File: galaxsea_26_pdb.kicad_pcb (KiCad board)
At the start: 2 copper layers, 235.7 x 148.4 mm, 92 parts, among them J1 XT-30, J10 XT-30, J11 Conn_01x36, J12 XT-30, J13 XT-30, J14 XT-30, J15 XT-30, J16 XT-30, J17 XT-30, J18 XT-30, J19 Conn_01x36, J2 XT-30, J20 XT-90, J21 Conn_01x36, J22 XT-30, J23 XT-30, J24 XT-30, J25 XT-30, J26 Conn_01x36, J27 XT-30, J28 XT-30, J29 XT-30, J3 Conn_01x36, J30 XT-30, J31 B2B-XH, J32 B2B-XH, J33 XT-30, J34 XT-60, J35 XT-60, J36 XT-60, J37 XT-60, J4 Conn_01x36, J5 Conn_01x36, J6 XT-30, J7 XT-90, J8 XT-30, J9 XT-30, U1 TPS54531DDA, U2 TPS54531DDA

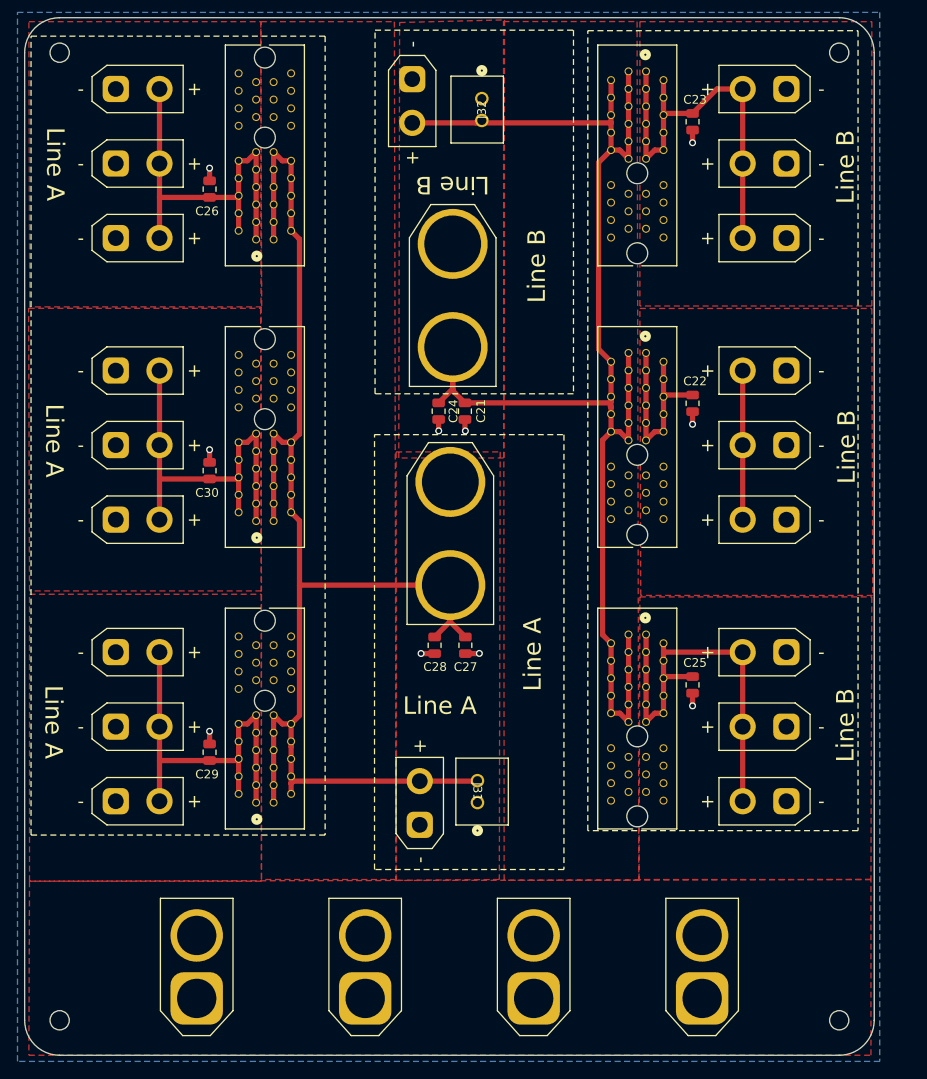
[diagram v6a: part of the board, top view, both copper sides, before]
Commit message: Switch ESC connectors to XT-30
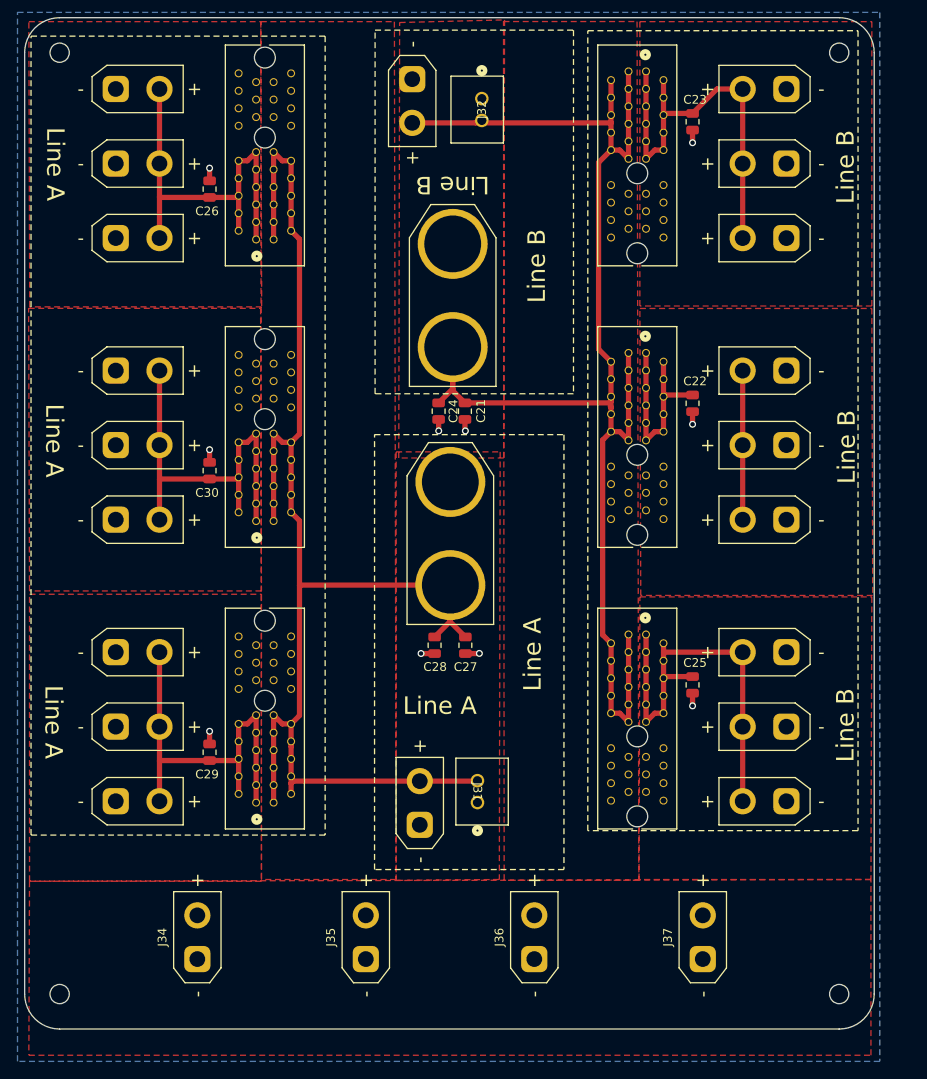
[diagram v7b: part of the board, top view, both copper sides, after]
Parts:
- J34, J35, J36, J37: value XT-60 -> XT-30; footprint footprints:AMASS_XT60-F_1x02_P7.20mm_Vertical -> Connector_AMASS:AMASS_XT30UPB-F_1x02_P5.0mm_Vertical
- moved J34 4.50 mm to (60.0, 161.4)
- moved J35 4.50 mm to (79.2, 161.4)
- moved J36 4.50 mm to (98.5, 161.4)
- moved J37 4.50 mm to (117.8, 161.4)
- moved H7 3.00 mm to (133.4, 165.4)
- moved H8 3.00 mm to (44.2, 165.4)
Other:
- board size 235.7 x 148.4 mm -> 235.7 x 145.4 mm
